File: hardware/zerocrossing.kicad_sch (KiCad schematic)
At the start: 7 parts

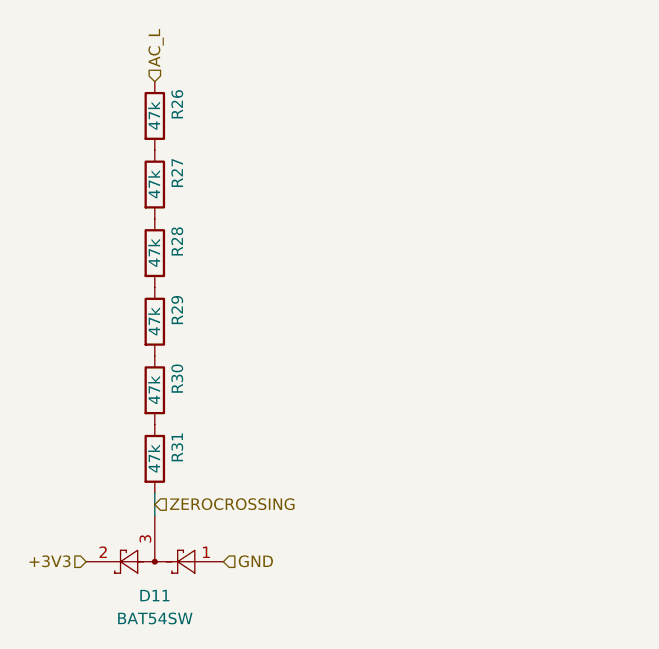
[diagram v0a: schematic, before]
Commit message: added some datasheets
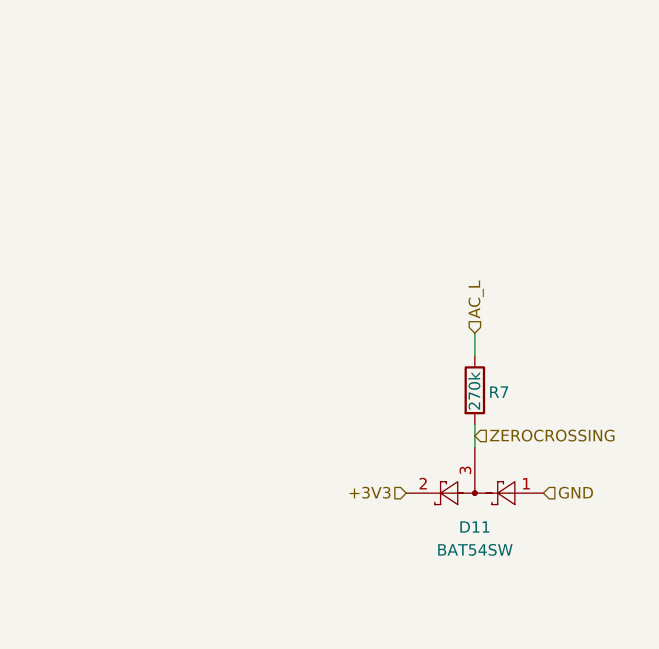
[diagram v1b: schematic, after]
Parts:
- removed R26, R27, R28, R29, R30, R31: 47k, Resistor_SMD:R_0603_1608Metric, symbol Device:R
- added R7: 270k, Resistor_SMD:R_MELF_MMB-0207, symbol Device:R
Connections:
- net AC_L: now also R7.1
- net ZEROCROSSING: now also R7.2
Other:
- moved on the sheet: D11

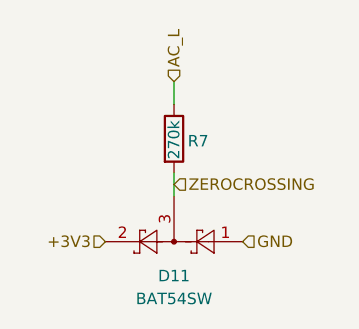
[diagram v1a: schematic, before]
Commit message: added testpoints. adjusted opamps for correct measurement. replaced hard resistors with potentiometer trimmers if necessary
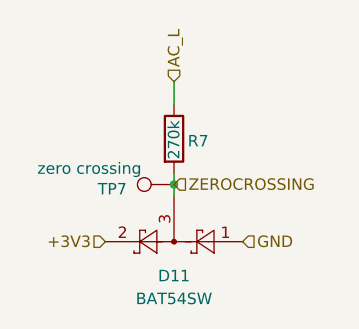
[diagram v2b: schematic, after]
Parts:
- added TP7: zero crossing, TestPoint:TestPoint_Pad_D1.0mm, symbol Connector:TestPoint
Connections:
- net ZEROCROSSING: now also TP7.1
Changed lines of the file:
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@@
 	(generator_version "8.0")
 	(paper "A4")
+	(junction
+		(at 147.32 92.71)
+		(diameter 0)
+		(color 0 0 0 0)
+	)
 	(wire
 		(pts
@@
 	(wire
 		(pts
-			(xy 147.32 93.98) (xy 147.32 91.44)
+			(xy 147.32 92.71) (xy 147.32 91.44)
+		)
+		(stroke
+			(width 0)
+			(type default)
+		)
+	)
+	(wire
+		(pts
+			(xy 147.32 93.98) (xy 147.32 92.71)
 		)
 		(stroke
@@
 					(unit 1)
 				)
+			)
+		)
+	)
+	(symbol
+		(lib_id "Connector:TestPoint")
+		(at 147.32 92.71 90)
+		(unit 1)
+		(exclude_from_sim no)
+		(in_bom yes)
+		(on_board yes)
+		(dnp no)
+		(property "Reference" "TP7"
+			(at 140.462 93.218 90)
+			(effects
+				(font
+					(size 1.27 1.27)
+				)
+			)
+		)
+		(property "Value" "zero crossing"
+			(at 137.922 90.932 90)
+			(effects
+				(font
+					(size 1.27 1.27)
+				)
+			)
+		)
+		(property "Footprint" "TestPoint:TestPoint_Pad_D1.0mm"
+			(at 147.32 87.63 0)
+			(effects
+				(font
+					(size 1.27 1.27)
+				)
+				(hide yes)
+			)
+		)
+		(property "Datasheet" "~"
+			(at 147.32 87.63 0)
+			(effects
+				(font
+					(size 1.27 1.27)
+				)
+				(hide yes)
+			)
+		)
+		(property "Description" "test point"
+			(at 147.32 92.71 0)
+			(effects
+				(font
+					(size 1.27 1.27)
+				)
+				(hide yes)
+			)
+		)
+		(pin "1"
+		)
+		(instances
+			(project "Steuerplatine"
+				(path "/ae153005-c1c4-4678-92de-98a47cf88e8d/07760232-15e4-46f9-95b3-fc11511709d6"
+					(reference "TP7")
+					(unit 1)
+				)
